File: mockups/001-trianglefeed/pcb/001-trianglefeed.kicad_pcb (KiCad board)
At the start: 2 copper layers, 62 x 130 mm, 10 parts, among them P1 SMA, P2 SMA

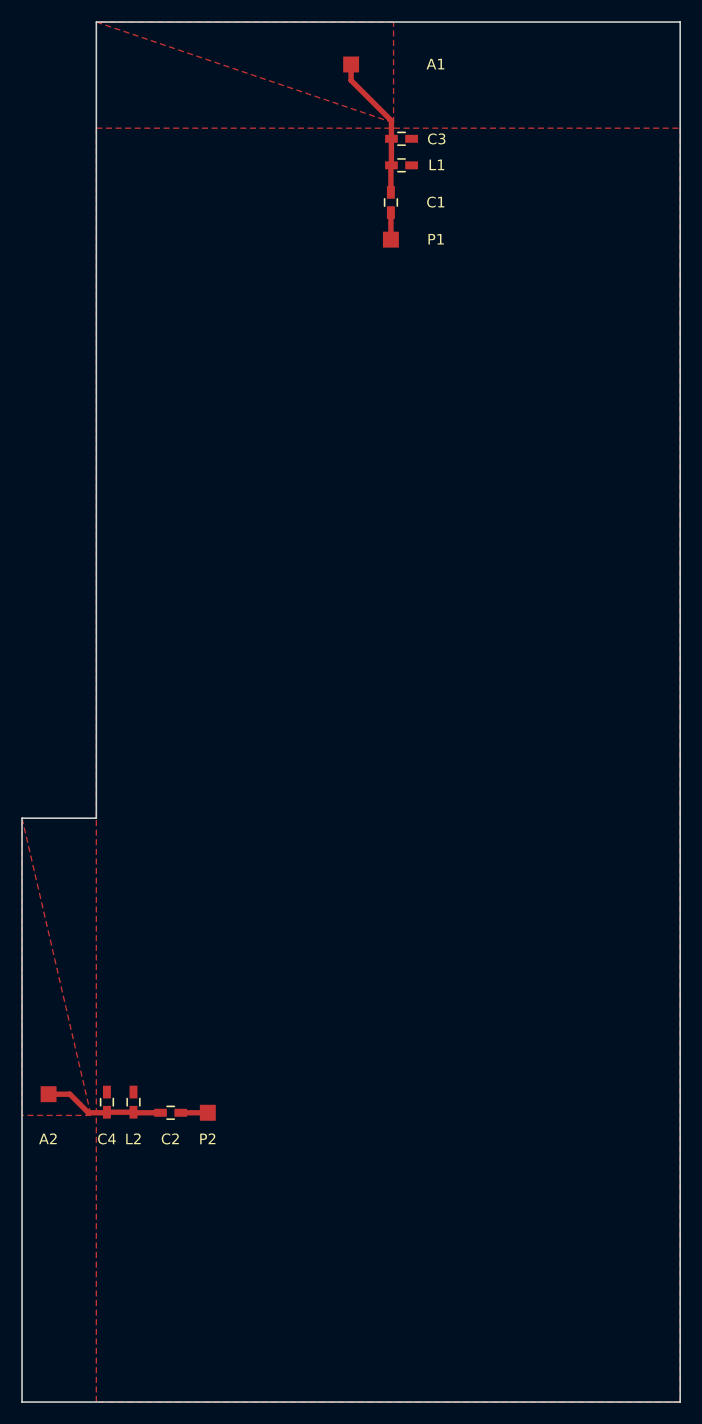
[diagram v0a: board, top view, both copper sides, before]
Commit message: Measurement of antenna.
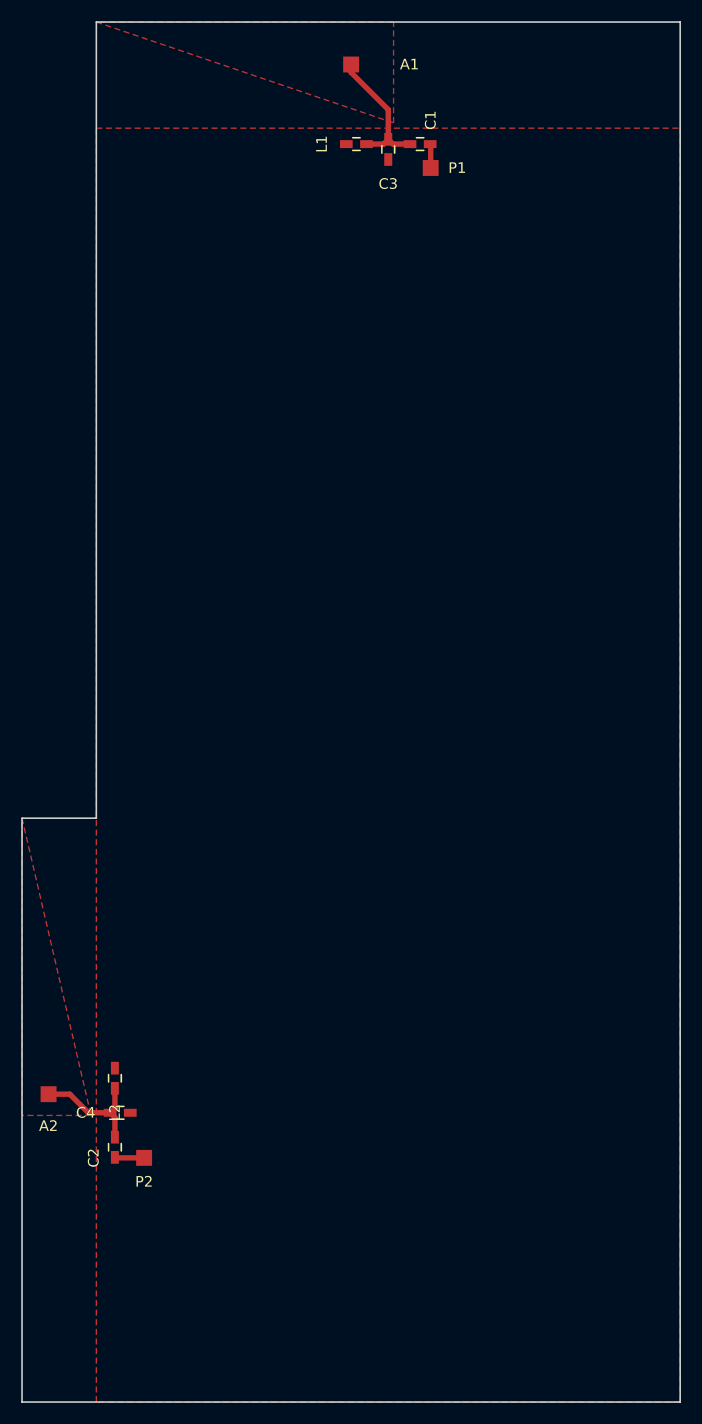
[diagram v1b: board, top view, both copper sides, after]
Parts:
- moved P1 7.72 mm to (91.5, 48.8)
- moved P2 7.35 mm to (64.5, 142.0)
- moved C2 6.17 mm to (61.8, 141.0), turned to 270 degrees
- moved C1 6.15 mm to (90.5, 46.5), turned to 0 degrees
- moved L1 4.70 mm to (84.5, 46.5), turned to 180 degrees
- moved L2 2.85 mm to (61.8, 134.5)
- moved C3 1.60 mm to (87.5, 47.0), turned to 270 degrees
- moved C4 1.60 mm to (62.2, 137.8), turned to 0 degrees
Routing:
- net /Ant1: track 13.6 -> 13.0 mm
